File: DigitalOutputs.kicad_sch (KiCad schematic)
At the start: 2 parts, among them J13 DIGITAL_OUTPUTS

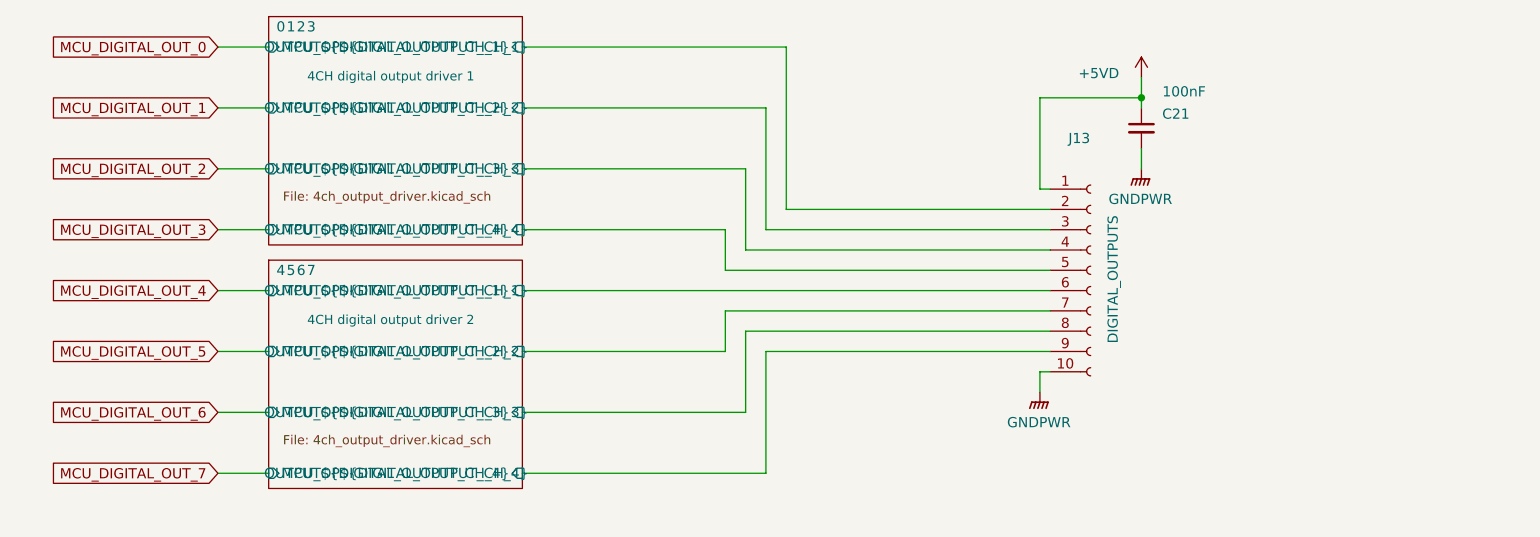
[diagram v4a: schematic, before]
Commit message: more BOM consolidation. Switched out IO for vertical toolless wire to board terminals and added footprints. Put new isolated ground plane on board.
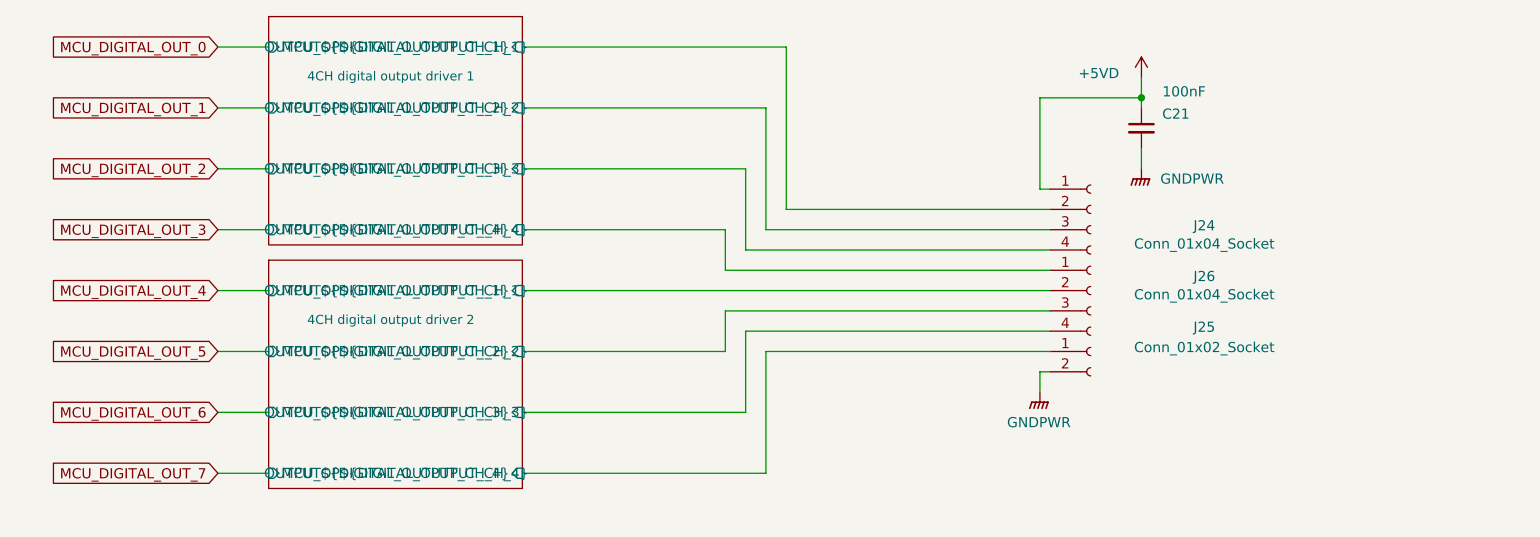
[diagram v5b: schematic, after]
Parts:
- removed J13: DIGITAL_OUTPUTS, EBWA_06_A:CONN_EBWA-10-A_ADM, symbol Connector:Conn_01x10_Socket
- added J24, J26: Conn_01x04_Socket, Amphenol QT:QT04ADP83V0000G, symbol Connector:Conn_01x04_Socket
- added J25: Conn_01x02_Socket, Amphenol QT:QT02ADP83V0000G, symbol Connector:Conn_01x02_Socket
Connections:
- net +5VD: now also J24.1 (Pin_1)
- net 4CH digital output driver 1/OUTPUT${DIGITAL_OUTPUT_CH_1}: now also J24.2 (Pin_2)
- net 4CH digital output driver 1/OUTPUT${DIGITAL_OUTPUT_CH_2}: now also J24.3 (Pin_3)
- net 4CH digital output driver 1/OUTPUT${DIGITAL_OUTPUT_CH_3}: now also J24.4 (Pin_4)
- net 4CH digital output driver 1/OUTPUT${DIGITAL_OUTPUT_CH_4}: now also J26.1 (Pin_1)
- net 4CH digital output driver 2/OUTPUT${DIGITAL_OUTPUT_CH_1}: now also J26.2 (Pin_2)
- net 4CH digital output driver 2/OUTPUT${DIGITAL_OUTPUT_CH_2}: now also J26.3 (Pin_3)
- net 4CH digital output driver 2/OUTPUT${DIGITAL_OUTPUT_CH_3}: now also J26.4 (Pin_4)
- net 4CH digital output driver 2/OUTPUT${DIGITAL_OUTPUT_CH_4}: now also J25.1 (Pin_1)
- net GNDPWR: now also J25.2 (Pin_2)
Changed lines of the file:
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@@
 		(on_board yes)
 		(dnp no)
-		(fields_autoplaced yes)
 		(property "Reference" "#PWR0123"
 			(at 212.09 86.36 0)
@@
 		)
 		(property "Value" "GNDPWR"
-			(at 211.963 85.09 0)
+			(at 218.44 82.55 0)
 			(effects
 				(font
@@
 				(path "/5473abc6-7b93-43cc-a401-f691c4d7d7cf/a10f9653-3098-46b3-8571-958500eea49a"
 					(reference "#PWR0123")
+					(unit 1)
+				)
+			)
+		)
+	)
+	(symbol
+		(lib_id "Connector:Conn_01x04_Socket")
+		(at 205.74 96.52 0)
+		(unit 1)
+		(exclude_from_sim no)
+		(in_bom yes)
+		(on_board yes)
+		(dnp no)
+		(property "Reference" "J26"
+			(at 219.964 94.742 0)
+			(effects
+				(font
+					(size 1.27 1.27)
+				)
+			)
+		)
+		(property "Value" "Conn_01x04_Socket"
+			(at 219.964 97.028 0)
+			(effects
+				(font
+					(size 1.27 1.27)
+				)
+			)
+		)
+		(property "Footprint" "Amphenol QT:QT04ADP83V0000G"
+			(at 205.74 96.52 0)
+			(effects
+				(font
+					(size 1.27 1.27)
+				)
+				(hide yes)
+			)
+		)
+		(property "Datasheet" "~"
+			(at 205.74 96.52 0)
+			(effects
+				(font
+					(size 1.27 1.27)
+				)
+				(hide yes)
+			)
+		)
+		(property "Description" "Generic connector, single row, 01x04, script generated"
+			(at 205.74 96.52 0)
+			(effects
+				(font
+					(size 1.27 1.27)
+				)
+				(hide yes)
+			)
+		)
+		(property "Digikey Part Number" "1818-QT02ADP83V0000G-ND"
+			(at 205.74 96.52 0)
+			(effects
+				(font
+					(size 1.27 1.27)
+				)
+				(hide yes)
+			)
+		)
+		(property "Digikey URL" "https://www.digikey.com.au/en/products/detail/amphenol-anytek/QT02ADP83V0000G/25618889"
+			(at 205.74 96.52 0)
+			(effects
+				(font
+					(size 1.27 1.27)
+				)
+				(hide yes)
+			)
+		)
+		(pin "3"
+		)
+		(pin "4"
+		)
+		(pin "2"
+		)
+		(pin "1"
+		)
+		(instances
+			(project "Remora Nucleo F446ZE Hat"
+				(path "/5473abc6-7b93-43cc-a401-f691c4d7d7cf/a10f9653-3098-46b3-8571-958500eea49a"
+					(reference "J26")
+					(unit 1)
+				)
+			)
+		)
+	)
+	(symbol
+		(lib_id "Connector:Conn_01x04_Socket")
+		(at 205.74 86.36 0)
+		(unit 1)
+		(exclude_from_sim no)
+		(in_bom yes)
+		(on_board yes)
+		(dnp no)
+		(property "Reference" "J24"
+			(at 219.964 88.392 0)
+			(effects
+				(font
+					(size 1.27 1.27)
+				)
+			)
+		)
+		(property "Value" "Conn_01x04_Socket"
+			(at 219.964 90.678 0)
+			(effects
+				(font
+					(size 1.27 1.27)
+				)
+			)
+		)
+		(property "Footprint" "Amphenol QT:QT04ADP83V0000G"
+			(at 205.74 86.36 0)
+			(effects
+				(font
+					(size 1.27 1.27)
+				)
+				(hide yes)
+			)
+		)
+		(property "Datasheet" "~"
+			(at 205.74 86.36 0)
+			(effects
+				(font
+					(size 1.27 1.27)
+				)
+				(hide yes)
+			)
+		)
+		(property "Description" "Generic connector, single row, 01x04, script generated"
+			(at 205.74 86.36 0)
+			(effects
+				(font
+					(size 1.27 1.27)
+				)
+				(hide yes)
+			)
+		)
+		(property "Digikey Part Number" "1818-QT02ADP83V0000G-ND"
+			(at 205.74 86.36 0)
+			(effects
+				(font
+					(size 1.27 1.27)
+				)
+				(hide yes)
+			)
+		)
+		(property "Digikey URL" "https://www.digikey.com.au/en/products/detail/amphenol-anytek/QT02ADP83V0000G/25618889"
+			(at 205.74 86.36 0)
+			(effects
+				(font
+					(size 1.27 1.27)
+				)
+				(hide yes)
+			)
+		)
+		(pin "3"
+		)
+		(pin "4"
+		)
+		(pin "2"
+		)
+		(pin "1"
+		)
+		(instances
+			(project "Remora Nucleo F446ZE Hat"
+				(path "/5473abc6-7b93-43cc-a401-f691c4d7d7cf/a10f9653-3098-46b3-8571-958500eea49a"
+					(reference "J24")
 					(unit 1)
 				)
@@
 	)
 	(symbol
-		(lib_id "Connector:Conn_01x10_Socket")
-		(at 205.74 93.98 0)
+		(lib_id "Connector:Conn_01x02_Socket")
+		(at 205.74 104.14 0)
 		(unit 1)
 		(exclude_from_sim no)
@@
 		(on_board yes)
 		(dnp no)
-		(property "Reference" "J13"
-			(at 202.946 77.47 0)
-			(effects
-				(font
-					(size 1.27 1.27)
-				)
-				(justify left)
-			)
-		)
-		(property "Value" "DIGITAL_OUTPUTS"
-			(at 208.534 103.124 90)
-			(effects
-				(font
-					(size 1.27 1.27)
-				)
-				(justify left)
-			)
-		)
-		(property "Footprint" "EBWA_06_A:CONN_EBWA-10-A_ADM"
-			(at 205.74 93.98 0)
+		(property "Reference" "J25"
+			(at 219.964 101.092 0)
+			(effects
+				(font
+					(size 1.27 1.27)
+				)
+			)
+		)
+		(property "Value" "Conn_01x02_Socket"
+			(at 219.964 103.632 0)
+			(effects
+				(font
+					(size 1.27 1.27)
+				)
+			)
+		)
+		(property "Footprint" "Amphenol QT:QT02ADP83V0000G"
+			(at 205.74 104.14 0)
 			(effects
 				(font
@@
 		)
 		(property "Datasheet" "~"
-			(at 205.74 93.98 0)
-			(effects
-				(font
-					(size 1.27 1.27)
-				)
-				(hide yes)
-			)
-		)
-		(property "Description" "Generic connector, single row, 01x10, script generated"
-			(at 205.74 93.98 0)
-			(effects
-				(font
-					(size 1.27 1.27)
-				)
-				(hide yes)
-			)
-		)
-		(property "Digikey Part Number" "See Manual BOM"
-			(at 205.74 93.98 0)
-			(effects
-				(font
-					(size 1.27 1.27)
-				)
-				(hide yes)
-			)
-		)
-		(property "Digikey URL" "See Manual BOM"
-			(at 205.74 93.98 0)
-			(effects
-				(font
-					(size 1.27 1.27)
-				)
-				(hide yes)
-			)
-		)
-		(pin "6"
-		)
-		(pin "8"
-		)
-		(pin "9"
+			(at 205.74 104.14 0)
+			(effects
+				(font
+					(size 1.27 1.27)
+				)
+				(hide yes)
+			)
+		)
+		(property "Description" "Generic connector, single row, 01x02, script generated"
+			(at 205.74 104.14 0)
+			(effects
+				(font
+					(size 1.27 1.27)
+				)
+				(hide yes)
+			)
+		)
+		(property "Digikey Part Number" "1818-QT04ADP83V0000G-ND"
+			(at 205.74 104.14 0)
+			(effects
+				(font
+					(size 1.27 1.27)
+				)
+				(hide yes)
+			)
+		)
+		(property "Digikey URL" "https://www.digikey.com.au/en/products/detail/amphenol-anytek/QT04ADP83V0000G/25618782"
+			(at 205.74 104.14 0)
+			(effects
+				(font
+					(size 1.27 1.27)
+				)
+				(hide yes)
+			)
 		)
 		(pin "1"
 		)
-		(pin "10"
-		)
-		(pin "7"
-		)
 		(pin "2"
-		)
-		(pin "3"
-		)
-		(pin "5"
-		)
-		(pin "4"
 		)
 		(instances
 			(project "Remora Nucleo F446ZE Hat"
 				(path "/5473abc6-7b93-43cc-a401-f691c4d7d7cf/a10f9653-3098-46b3-8571-958500eea49a"
-					(reference "J13")
+					(reference "J25")
 					(unit 1)
 				)
@@
 				)
 				(justify left top)
+				(hide yes)
 			)
 		)
@@
 					(size 1.27 1.27)
 				)
+				(hide yes)
 			)
 		)
@@
 					(size 1.27 1.27)
 				)
+				(hide yes)
 			)
 		)
@@
 					(size 1.27 1.27)
 				)
+				(hide yes)
 			)
 		)
@@
 					(size 1.27 1.27)
 				)
+				(hide yes)
 			)
 		)
@@
 				)
 				(justify left top)
+				(hide yes)
 			)
 		)
@@
 					(size 1.27 1.27)
 				)
+				(hide yes)
 			)
 		)
@@
 					(size 1.27 1.27)
 				)
+				(hide yes)
 			)
 		)
@@
 					(size 1.27 1.27)
 				)
+				(hide yes)
 			)
 		)
@@
 					(size 1.27 1.27)
 				)
-			)
-		)
+				(hide yes)
+			)
+		)

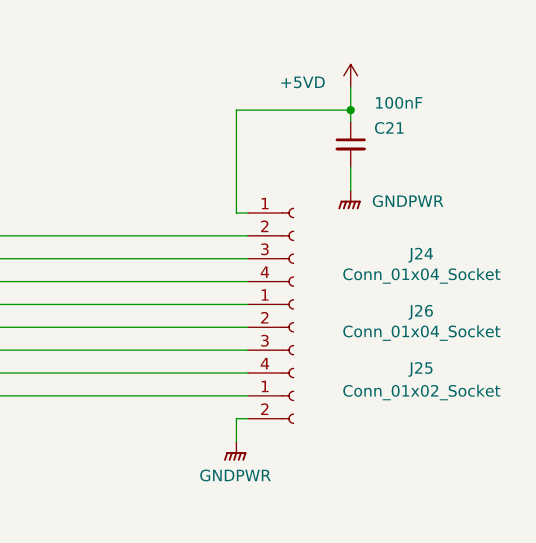
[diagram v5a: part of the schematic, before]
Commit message: New PSU designs + footprints assigned. Changes to board shape to make room for new components. BOM consolidation of supplimentary file
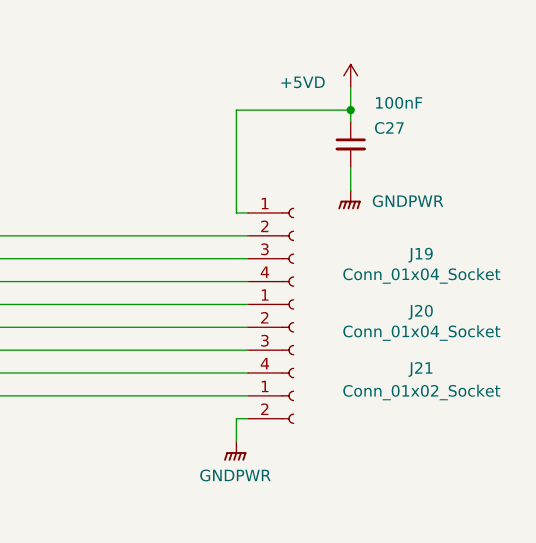
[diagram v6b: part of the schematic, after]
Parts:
- J19: renamed from J24; Digikey Part Number 1818-QT02ADP83V0000G-ND -> 1818-QT04ADP83V0000G-ND; Digikey URL https://www.digikey.com.au/en/products/detail/amphenol-anytek/QT02ADP83V0000G/25618889 -> https://www.digikey.com.au/en/products/detail/amphenol-anytek/QT04ADP83V0000G/25618782
- J20: renamed from J26; Digikey Part Number 1818-QT02ADP83V0000G-ND -> 1818-QT04ADP83V0000G-ND; Digikey URL https://www.digikey.com.au/en/products/detail/amphenol-anytek/QT02ADP83V0000G/25618889 -> https://www.digikey.com.au/en/products/detail/amphenol-anytek/QT04ADP83V0000G/25618782
- J21: renamed from J25; Digikey Part Number 1818-QT04ADP83V0000G-ND -> 1818-QT02ADP83V0000G-ND; Digikey URL https://www.digikey.com.au/en/products/detail/amphenol-anytek/QT04ADP83V0000G/25618782 -> https://www.digikey.com.au/en/products/detail/amphenol-anytek/QT02ADP83V0000G/25618889
- renumbered C21 to C27
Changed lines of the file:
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@@
 		(on_board yes)
 		(dnp no)
-		(property "Reference" "C21"
+		(property "Reference" "C27"
 			(at 216.408 74.422 0)
 			(effects
@@
 			(project "Remora Nucleo F446ZE Hat"
 				(path "/5473abc6-7b93-43cc-a401-f691c4d7d7cf/a10f9653-3098-46b3-8571-958500eea49a"
-					(reference "C21")
+					(reference "C27")
 					(unit 1)
 				)
@@
 		(on_board yes)
 		(dnp no)
-		(property "Reference" "#PWR0123"
+		(property "Reference" "#PWR0192"
 			(at 212.09 86.36 0)
 			(effects
@@
 			(project "Remora Nucleo F446ZE Hat"
 				(path "/5473abc6-7b93-43cc-a401-f691c4d7d7cf/a10f9653-3098-46b3-8571-958500eea49a"
-					(reference "#PWR0123")
+					(reference "#PWR0192")
 					(unit 1)
 				)
@@
 		(on_board yes)
 		(dnp no)
-		(property "Reference" "J26"
+		(property "Reference" "J20"
 			(at 219.964 94.742 0)
 			(effects
@@
 			)
 		)
-		(property "Digikey Part Number" "1818-QT02ADP83V0000G-ND"
+		(property "Digikey Part Number" "1818-QT04ADP83V0000G-ND"
 			(at 205.74 96.52 0)
 			(effects
@@
 			)
 		)
-		(property "Digikey URL" "https://www.digikey.com.au/en/products/detail/amphenol-anytek/QT02ADP83V0000G/25618889"
+		(property "Digikey URL" "https://www.digikey.com.au/en/products/detail/amphenol-anytek/QT04ADP83V0000G/25618782"
 			(at 205.74 96.52 0)
 			(effects
@@
 			(project "Remora Nucleo F446ZE Hat"
 				(path "/5473abc6-7b93-43cc-a401-f691c4d7d7cf/a10f9653-3098-46b3-8571-958500eea49a"
-					(reference "J26")
+					(reference "J20")
 					(unit 1)
 				)
@@
 		(on_board yes)
 		(dnp no)
-		(property "Reference" "J24"
+		(property "Reference" "J19"
 			(at 219.964 88.392 0)
 			(effects
@@
 			)
 		)
-		(property "Digikey Part Number" "1818-QT02ADP83V0000G-ND"
+		(property "Digikey Part Number" "1818-QT04ADP83V0000G-ND"
 			(at 205.74 86.36 0)
 			(effects
@@
 			)
 		)
-		(property "Digikey URL" "https://www.digikey.com.au/en/products/detail/amphenol-anytek/QT02ADP83V0000G/25618889"
+		(property "Digikey URL" "https://www.digikey.com.au/en/products/detail/amphenol-anytek/QT04ADP83V0000G/25618782"
 			(at 205.74 86.36 0)
 			(effects
@@
 			(project "Remora Nucleo F446ZE Hat"
 				(path "/5473abc6-7b93-43cc-a401-f691c4d7d7cf/a10f9653-3098-46b3-8571-958500eea49a"
-					(reference "J24")
+					(reference "J19")
 					(unit 1)
 				)
@@
 		(dnp no)
 		(fields_autoplaced yes)
-		(property "Reference" "#PWR0121"
+		(property "Reference" "#PWR0190"
 			(at 199.39 114.3 0)
 			(effects
@@
 			(project ""
 				(path "/5473abc6-7b93-43cc-a401-f691c4d7d7cf/a10f9653-3098-46b3-8571-958500eea49a"
-					(reference "#PWR0121")
+					(reference "#PWR0190")
 					(unit 1)
 				)
@@
 		(on_board yes)
 		(dnp no)
-		(property "Reference" "#PWR0122"
+		(property "Reference" "#PWR0191"
 			(at 212.09 73.66 0)
 			(effects
@@
 			(project "Remora Nucleo F446ZE Hat"
 				(path "/5473abc6-7b93-43cc-a401-f691c4d7d7cf/a10f9653-3098-46b3-8571-958500eea49a"
-					(reference "#PWR0122")
+					(reference "#PWR0191")
 					(unit 1)
 				)
@@
 		(on_board yes)
 		(dnp no)
-		(property "Reference" "J25"
+		(property "Reference" "J21"
 			(at 219.964 101.092 0)
 			(effects
@@
 			)
 		)
-		(property "Digikey Part Number" "1818-QT04ADP83V0000G-ND"
+		(property "Digikey Part Number" "1818-QT02ADP83V0000G-ND"
 			(at 205.74 104.14 0)
 			(effects
@@
 			)
 		)
-		(property "Digikey URL" "https://www.digikey.com.au/en/products/detail/amphenol-anytek/QT04ADP83V0000G/25618782"
+		(property "Digikey URL" "https://www.digikey.com.au/en/products/detail/amphenol-anytek/QT02ADP83V0000G/25618889"
 			(at 205.74 104.14 0)
 			(effects
@@
 			(project "Remora Nucleo F446ZE Hat"
 				(path "/5473abc6-7b93-43cc-a401-f691c4d7d7cf/a10f9653-3098-46b3-8571-958500eea49a"
-					(reference "J25")
-					(unit 1)
-				)
+					(reference "J21")
+					(unit 1)
+				)

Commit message: Added Analog inputs, updates to readme re powering board from external supply
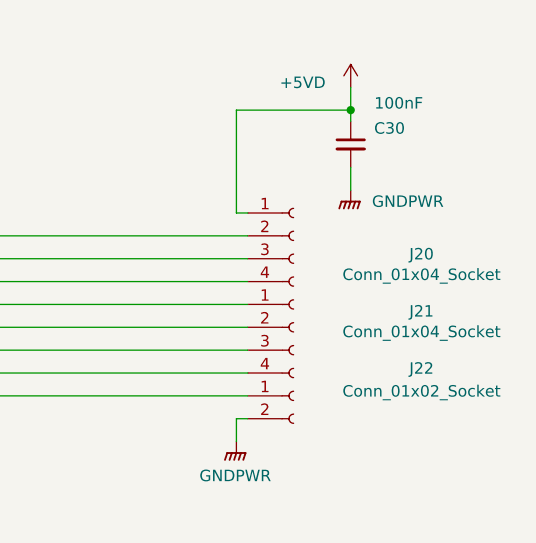
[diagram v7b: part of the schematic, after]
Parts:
- renumbered C27 to C30, J19 to J20, J20 to J21, J21 to J22
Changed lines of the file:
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@@
 		(on_board yes)
 		(dnp no)
-		(property "Reference" "C27"
+		(property "Reference" "C30"
 			(at 216.408 74.422 0)
 			(effects
@@
 			(project "Remora Nucleo F446ZE Hat"
 				(path "/5473abc6-7b93-43cc-a401-f691c4d7d7cf/a10f9653-3098-46b3-8571-958500eea49a"
-					(reference "C27")
+					(reference "C30")
 					(unit 1)
 				)
@@
 		(on_board yes)
 		(dnp no)
-		(property "Reference" "#PWR0192"
+		(property "Reference" "#PWR0201"
 			(at 212.09 86.36 0)
 			(effects
@@
 			(project "Remora Nucleo F446ZE Hat"
 				(path "/5473abc6-7b93-43cc-a401-f691c4d7d7cf/a10f9653-3098-46b3-8571-958500eea49a"
-					(reference "#PWR0192")
+					(reference "#PWR0201")
 					(unit 1)
 				)
@@
 		(on_board yes)
 		(dnp no)
-		(property "Reference" "J20"
+		(property "Reference" "J21"
 			(at 219.964 94.742 0)
 			(effects
@@
 			(project "Remora Nucleo F446ZE Hat"
 				(path "/5473abc6-7b93-43cc-a401-f691c4d7d7cf/a10f9653-3098-46b3-8571-958500eea49a"
-					(reference "J20")
+					(reference "J21")
 					(unit 1)
 				)
@@
 		(on_board yes)
 		(dnp no)
-		(property "Reference" "J19"
+		(property "Reference" "J20"
 			(at 219.964 88.392 0)
 			(effects
@@
 			(project "Remora Nucleo F446ZE Hat"
 				(path "/5473abc6-7b93-43cc-a401-f691c4d7d7cf/a10f9653-3098-46b3-8571-958500eea49a"
-					(reference "J19")
+					(reference "J20")
 					(unit 1)
 				)
@@
 		(dnp no)
 		(fields_autoplaced yes)
-		(property "Reference" "#PWR0190"
+		(property "Reference" "#PWR0199"
 			(at 199.39 114.3 0)
 			(effects
@@
 			(project ""
 				(path "/5473abc6-7b93-43cc-a401-f691c4d7d7cf/a10f9653-3098-46b3-8571-958500eea49a"
-					(reference "#PWR0190")
+					(reference "#PWR0199")
 					(unit 1)
 				)
@@
 		(on_board yes)
 		(dnp no)
-		(property "Reference" "#PWR0191"
+		(property "Reference" "#PWR0200"
 			(at 212.09 73.66 0)
 			(effects
@@
 			(project "Remora Nucleo F446ZE Hat"
 				(path "/5473abc6-7b93-43cc-a401-f691c4d7d7cf/a10f9653-3098-46b3-8571-958500eea49a"
-					(reference "#PWR0191")
+					(reference "#PWR0200")
 					(unit 1)
 				)
@@
 		(on_board yes)
 		(dnp no)
-		(property "Reference" "J21"
+		(property "Reference" "J22"
 			(at 219.964 101.092 0)
 			(effects
@@
 			(project "Remora Nucleo F446ZE Hat"
 				(path "/5473abc6-7b93-43cc-a401-f691c4d7d7cf/a10f9653-3098-46b3-8571-958500eea49a"
-					(reference "J21")
-					(unit 1)
-				)
+					(reference "J22")
+					(unit 1)
+				)
